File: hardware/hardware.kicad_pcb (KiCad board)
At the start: 2 copper layers, 49.7 x 46.9 mm, 31 parts, among them J1 Conn_02x03_Odd_Even, U1 CH32V003FxPx

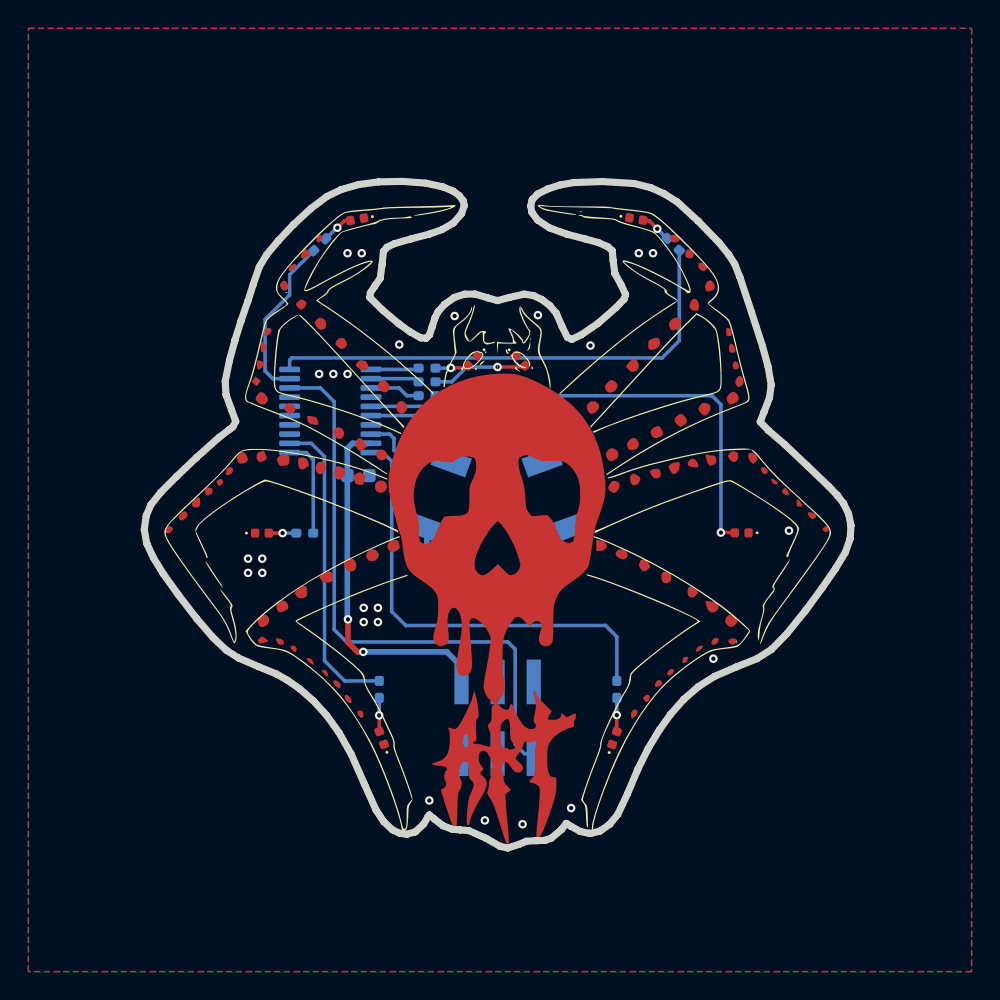
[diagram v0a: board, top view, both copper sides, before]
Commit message: feat: change routes and components place
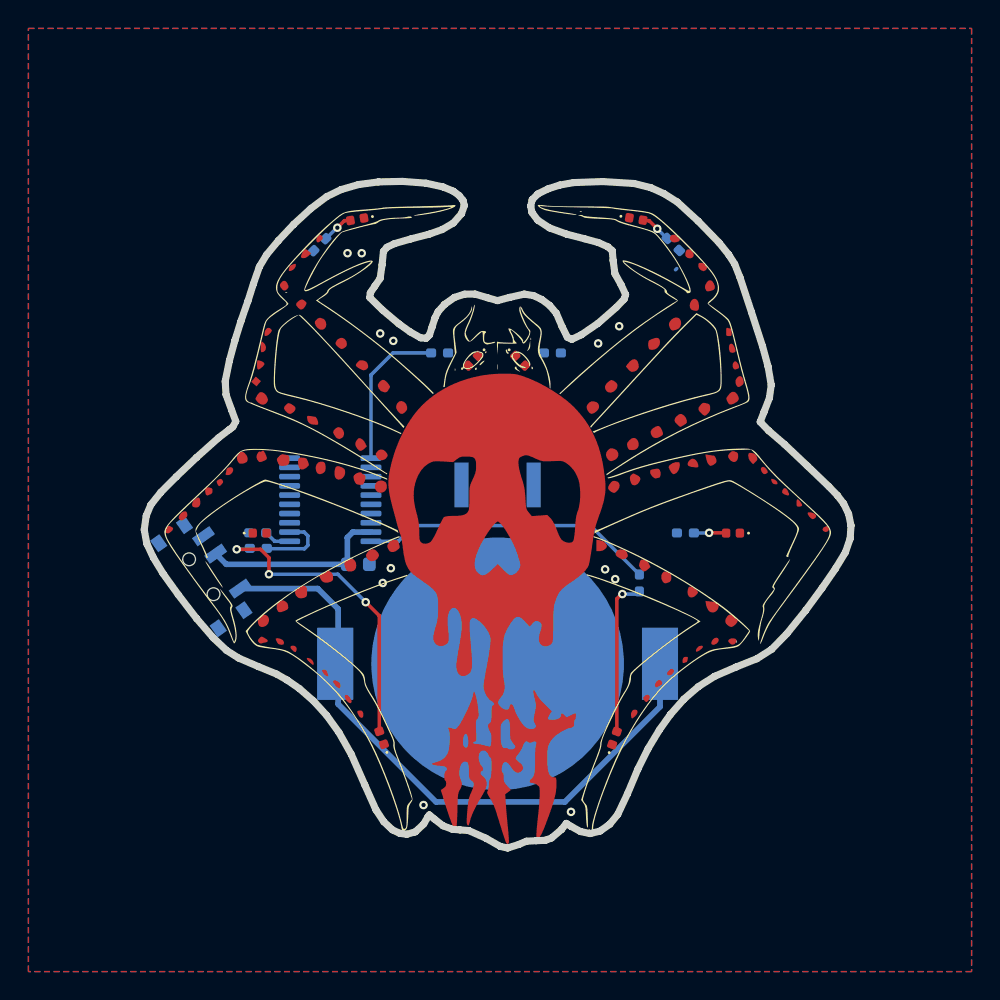
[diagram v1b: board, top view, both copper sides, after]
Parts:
- removed D1, D2, D3: LED, footprints:LYT77K-K2M1
- removed R1, R2, R3: 330, Resistor_SMD:R_0402_1005Metric_Pad0.72x0.64mm_HandSolder
- removed Ref**: Val**, footprints:front_eyes
- removed Ref**: Val**, footprints:drawing
- added BT1: Battery, footprints:BAT-HLD-001, B.Cu at (113.6, 72.9)
- added SW1: SW_SPST, Button_Switch_SMD:SW_SPDT_PCM12, B.Cu at (93.0, 66.6)
- R4, R5: value 330 -> 680
- moved R9 20.6 mm to (126.8, 63.7)
- moved J1 18.9 mm to (113.6, 57.8)
- moved kibuzzard-6986EFDC 15.7 mm to (142.3, 52.0)
- moved kibuzzard-6986EFC1 13.8 mm to (132.0, 81.8)
- moved R11 13.1 mm to (96.7, 64.8), turned to 0 degrees
- moved kibuzzard-6986EF7D 9.73 mm to (100.1, 78.5)
- moved kibuzzard-6986EFAB 9.22 mm to (100.0, 82.5)
- moved R5 9.05 mm to (117.4, 51.0), turned to 0 degrees
- moved R10 7.66 mm to (123.5, 67.2)
- moved U1 6.25 mm to (101.8, 61.4)
- moved C1 6.24 mm to (103.8, 65.9)
- moved R8 3.31 mm to (96.7, 63.7)
- moved R4 1.38 mm to (109.5, 51.0)
- moved D9 0.61 mm to (130.1, 63.7)
- moved D8 0.17 mm to (96.8, 63.7)
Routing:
- net Net-(BT1-+): track 0.00 -> 45.7 mm
- net /SWDIO: track 41.2 -> 0.00 mm
- net /LED_4: track 35.0 -> 0.00 mm
- net Net-(D9-A): track 30.3 -> 2.28 mm
- net Net-(D11-A): track 2.36 -> 21.7 mm, vias 1 -> 3
- net /NOSE: track 17.4 -> 0.00 mm
- net /LED_8: track 21.7 -> 5.07 mm
- net /RIGHT_EYE: track 15.6 -> 0.00 mm
- net +3.3V: track 25.3 -> 13.3 mm, vias 2 -> 0
- net /LED_3: track 11.8 -> 0.00 mm
- net /LED_7: track 32.0 -> 20.8 mm
- net Net-(D10-A): track 2.38 -> 11.1 mm
- net /LED_1: track 3.39 -> 10.9 mm
- net Net-(D5-A): track 6.77 -> 0.00 mm, vias 1 -> 0
- net Net-(D1-K): track 5.34 -> 0.00 mm
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
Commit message: feat: add routes and update hardware
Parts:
- added kibuzzard-6AD7C383: G***, kibuzzard-6AD7C383, B.Cu at (98.3, 68.3)
- moved kibuzzard-6986EFC1 25.3 mm to (118.7, 60.3)
- moved kibuzzard-6986EF7D 24.6 mm to (108.4, 55.3)
- moved kibuzzard-6986EFAB 23.8 mm to (108.4, 60.3)
- moved R9 19.1 mm to (107.7, 62.2)
- moved kibuzzard-6986EFDC 16.2 mm to (126.1, 52.0)
- turned D8 to 180 degrees
- turned U1 to 0 degrees
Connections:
- U1 pad 1: /LED_1 -> /LED_8
- U1 pad 10: /LED_7 -> /LED_4
- U1 pad 11: /LED_5 -> unconnected-(U1-PC1-Pad11)
- U1 pad 12: /LED_8 -> unconnected-(U1-PC2-Pad12)
- U1 pad 17: unconnected-(U1-PC7-Pad17) -> /LED_6
- U1 pad 19: /LED_3 -> /LED_7
- U1 pad 2: /LED_2 -> /LED_5
- U1 pad 20: /LED_4 -> unconnected-(U1-PD3-Pad20)
- U1 pad 3: /LED_6 -> /LED_3
- U1 pad 4: unconnected-(U1-PD7-Pad4) -> /LED_1
- U1 pad 5: /RIGHT_EYE -> /LED_2
- U1 pad 6: /NOSE -> unconnected-(U1-PA2-Pad6)
- U1 pad 8: /LEFT_EYE -> unconnected-(U1-PD0-Pad8)
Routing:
- net /LED_4: track 0.00 -> 40.7 mm
- net /LED_2: track 0.00 -> 32.2 mm
- net Net-(D9-A): track 2.28 -> 30.1 mm
- net /LED_3: track 0.00 -> 24.9 mm
- net +3.3V: track 13.3 -> 32.0 mm
- net /LED_1: track 10.9 -> 24.8 mm
- net /SWDIO: track 0.00 -> 13.8 mm
- net /LED_8: track 5.07 -> 1.81 mm
- net /LED_6: track 0.00 -> 2.53 mm
- net Net-(D8-A): track 0.00 -> 2.09 mm, vias 0 -> 1
- net Net-(D4-A): track 0.00 -> 1.89 mm, vias 0 -> 2
- net Net-(D5-A): track 0.00 -> 1.71 mm, vias 0 -> 1
- net /LED_7: track 20.8 -> 21.7 mm
- net GND: vias 12 -> 21
